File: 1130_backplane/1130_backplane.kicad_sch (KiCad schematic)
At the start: 0 parts

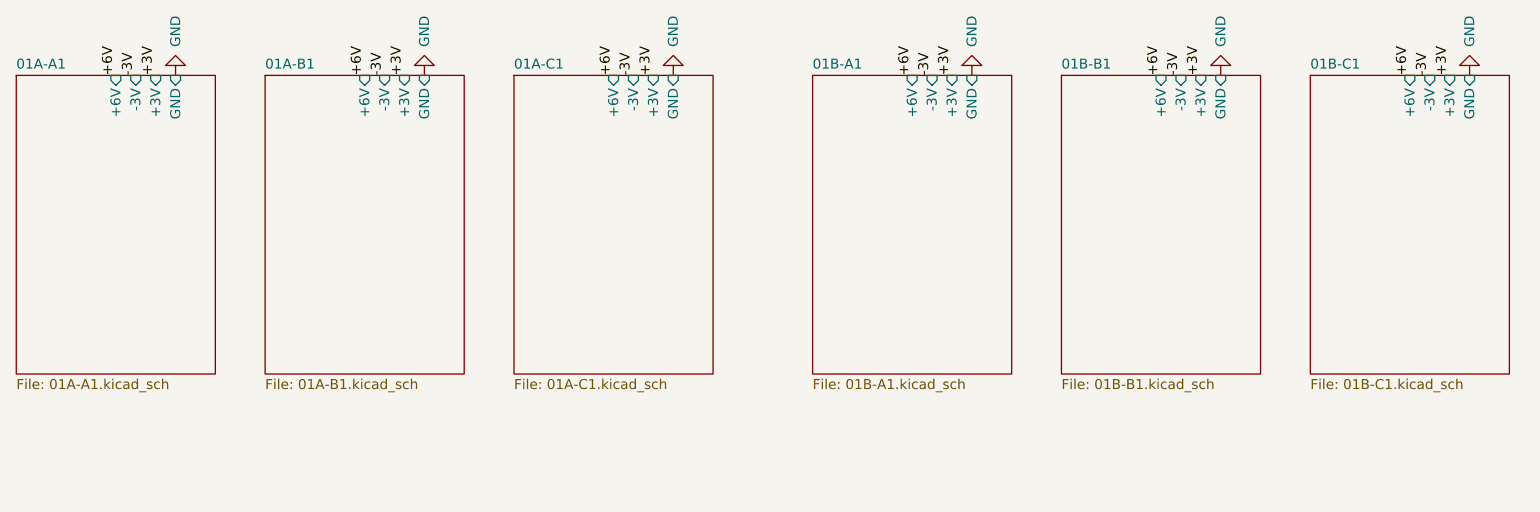
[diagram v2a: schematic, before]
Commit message: Finish page KA101-KA111
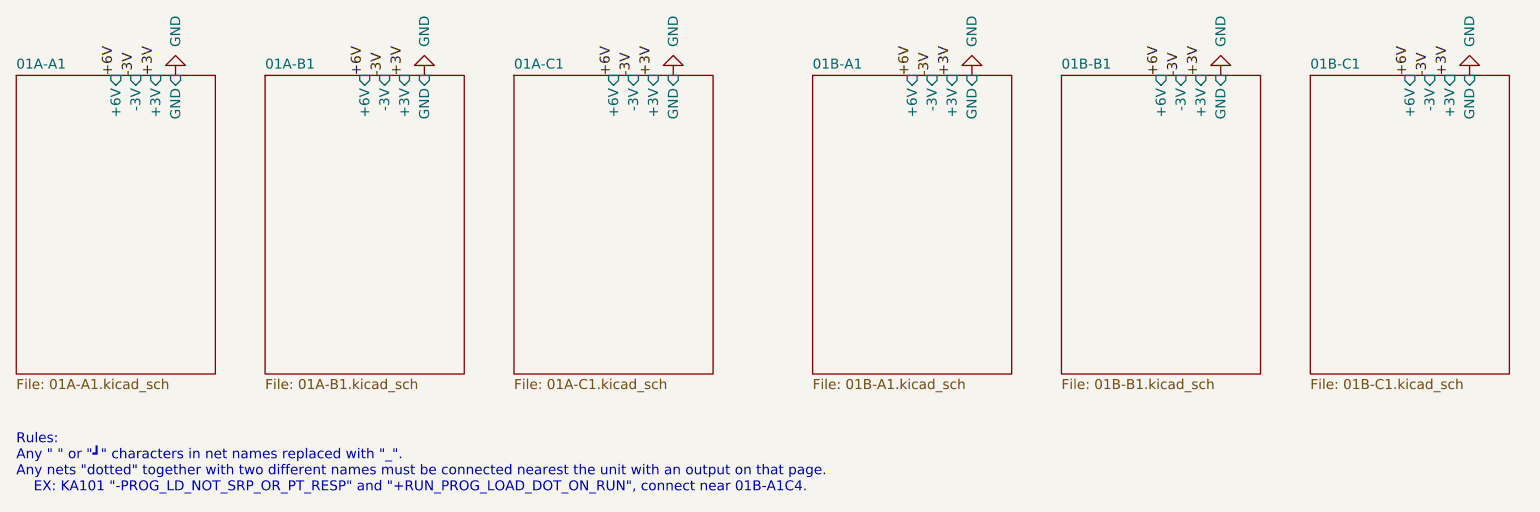
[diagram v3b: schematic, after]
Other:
- note added: "Rules: Any " " or "┛" characters in net names replaced with "_". Any nets "dotted" together with two different names must be connected nearest the unit with an output on that page. EX: KA101 "-PROG_LD_NOT_SRP_OR_PT_RESP" and "+RUN_PROG_LOAD_DOT_ON_RUN", connect near 01B-A1C4."
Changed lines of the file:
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@@
 (kicad_sch (version 20211123) (generator eeschema)
   (paper "A4")
+  (text "Rules:\nAny \" \" or \"┛\" characters in net names replaced with \"_\".\nAny nets \"dotted\" together with two different names must be connected nearest the unit with an output on that page.\n	EX: KA101 \"-PROG_LD_NOT_SRP_OR_PT_RESP\" and \"+RUN_PROG_LOAD_DOT_ON_RUN\", connect near 01B-A1C4."
+    (at 25.4 78.74 0)
+    (effects (font (size 1.27 1.27)) (justify left bottom))
+  )
   (label "-3V" (at 173.99 25.4 90)
     (effects (font (size 1.27 1.27)) (justify left bottom))

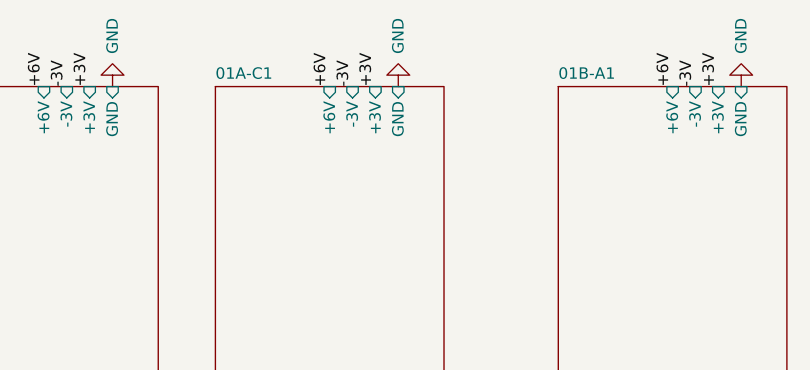
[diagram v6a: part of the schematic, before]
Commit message: Finish page KW101. Add 48V bus for 01A-C1
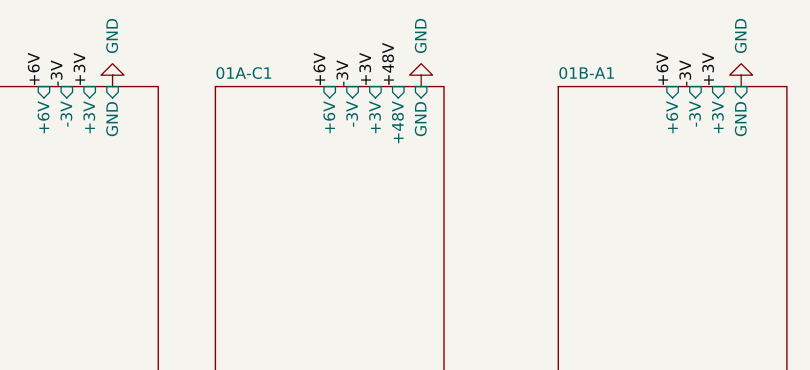
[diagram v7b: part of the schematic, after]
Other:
- sheet 01A-C1 ports: added +48V; removed none
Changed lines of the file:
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@@
+    (effects (font (size 1.27 1.27)) (justify left bottom))
+  )
+  (label "+48V" (at 109.22 25.4 90)
     (effects (font (size 1.27 1.27)) (justify left bottom))
   )
@@
     (pin "1")
   )
-  (symbol (lib_id "power:GND") (at 109.22 25.4 180) (unit 1)
-    (in_bom yes) (on_board yes)
-    (property "Reference" "#PWR03" (id 0) (at 109.22 19.05 0)
-      (effects (font (size 1.27 1.27)) hide)
-    )
-    (property "Value" "GND" (id 1) (at 109.22 17.78 90)
-      (effects (font (size 1.27 1.27)) (justify left))
-    )
-    (property "Footprint" "" (id 2) (at 109.22 25.4 0)
-      (effects (font (size 1.27 1.27)) hide)
-    )
-    (property "Datasheet" "" (id 3) (at 109.22 25.4 0)
+  (symbol (lib_id "power:GND") (at 111.76 25.4 180) (unit 1)
+    (in_bom yes) (on_board yes)
+    (property "Reference" "#PWR03" (id 0) (at 111.76 19.05 0)
+      (effects (font (size 1.27 1.27)) hide)
+    )
+    (property "Value" "GND" (id 1) (at 111.76 17.78 90)
+      (effects (font (size 1.27 1.27)) (justify left))
+    )
+    (property "Footprint" "" (id 2) (at 111.76 25.4 0)
+      (effects (font (size 1.27 1.27)) hide)
+    )
+    (property "Datasheet" "" (id 3) (at 111.76 25.4 0)
       (effects (font (size 1.27 1.27)) hide)
     )
@@
       (effects (font (size 1.27 1.27)) (justify right))
     )
-    (pin "GND" input (at 109.22 25.4 90)
-      (effects (font (size 1.27 1.27)) (justify right))
-    )
+    (pin "GND" input (at 111.76 25.4 90)
+      (effects (font (size 1.27 1.27)) (justify right))
+    )
+    (pin "+48V" input (at 109.22 25.4 90)
+      (effects (font (size 1.27 1.27)) (justify right))
+    )
